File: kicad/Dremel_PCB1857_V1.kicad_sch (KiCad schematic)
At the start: 34 parts, among them P1 Conn_WallPlug, U1 EL817

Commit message: Add Tested parameter to schematics
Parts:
- *R6: Tested (none) -> BLOWN
- C2: renamed from *C2; Tested (none) -> BLOWN
- C3: value 1n -> 100n
- R11, R15: value R -> 510k; Tested (none) -> OK
- R12, R13: value R -> 300k
- R14: Tested (none) -> OK
- R4: value R -> 47k; Tested (none) -> OK
- R6: value R -> 30R; Tested (none) -> BLOWN 3k4
- R7: value R -> 160R; Tested (none) -> OK
- R8: value R -> 4R7; Tested (none) -> OK
- U1: value EL817 -> B179
- V11: renamed from *D7; value D -> IN4007; Tested (none) -> OK
- V5, V6: Tested (none) -> FAULTY
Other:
- moved on the sheet: R14, TR1_*L1

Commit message: Added secondary side to schematic
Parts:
- added *: 220u 25V, symbol Device:C_Polarized
- added * (x4), V14: D, symbol Device:D
- added *: 470u 25V, symbol Device:C_Polarized
- added BT1: Battery_Cell, symbol Device:Battery_Cell
- added C12: 1n, symbol Device:C
- added C13: 100n, symbol Device:C
- added C14: 10n, symbol Device:C
- added C15: 2.2 n, symbol Device:C
- added C6, C7, C8: C, symbol Device:C
- added C9: ~, symbol Device:C
- added N2: TL1431A, Package_SO:SOIC-8_3.9x4.9mm_P1.27mm, symbol Reference_Voltage:TL431D
- added R*, R17, R25, R31, R46, R47: ~, symbol Device:R
- added R12, R16, R18, R20, R22, R23, R29, R33, R40, R41, R42, R43, R44: R, symbol Device:R
- added R20: 2k, symbol Device:R
- added R24: 1k, symbol Device:R
- added R26: O.22 R, symbol Device:R
- added R27: 0.22 R, symbol Device:R
- added R28, R32: 10k, symbol Device:R
- added R34: 20k, symbol Device:R
- added R35: 6.04k, symbol Device:R
- added R36: 25.5k, symbol Device:R
- added R37: 12k, symbol Device:R
- added R38: 29.4k, symbol Device:R
- added R39: 360R, symbol Device:R
- added TH1: Thermistor_PTC, symbol Device:Thermistor_PTC
- added TR1_*L3: 13.63 uH 0.28 R, symbol Device:L
- added TR1_*L4: 9.77 uH 0.05 R, symbol Device:L
- added U3: LM324, symbol Amplifier_Operational:LM324
- added V12: BC546A, Package_TO_SOT_THT:TO-92_Inline, symbol Transistor_BJT:BC546
- added V15: LED, symbol Device:LED
- added V201: FKH382N, symbol Device:Q_NMOS_SGD
- L1: value L_Coupled_1423 -> 16m H 0.7 R
- TR1_*L1: value 9u31 R17 -> 9.31 uH 0.17 R
- TR1_*L2: value 3m16 2R82 -> 3.16 mH 2.82 R
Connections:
- net at *D1.2 (A), *D4.2 (A), *R6.2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: now also C6.1
- net at U1.1: now also R12.2
- net BAT-: now reaches U1.2
- net BAT-: now also *.2, BT1.2 (-), C13.2, C7.2, N2.2 (A), N2.3 (A), N2.6 (A), N2.7 (A), R23.1, R26.1, R27.1, R36.1, R43.2, TR1_*L3.1, U3.10 (+), U3.11 (V-), U3.12 (+), U3.5 (+), V15.1 (K), V201.1 (S)
- new net: C12.2, N2.8 (REF), R22.1, R23.2, R29.2
- new net: *.2 (A), C9.1, TR1_*L4.2
- new net: *.1, *.1 (K), *.2 (A), R17.2, R34.2, R46.1, R47.2
- new net: R24.1, R28.2, U3.13 (-)
- new net: R28.1, R32.2, U3.14
- new net: *.1 (K), R16.1, R18.1
- new net: *.2 (A), C8.2, TR1_*L3.2
- new net: *.1 (K), R12.1, V14.1 (K)
- new net: C15.2, U3.1, V14.2 (A)
- new net: *.2 (A), C14.1, U3.8
- new net: C14.2, R20.1
- new net: C8.1, R16.2
- new net: C12.1, N2.1 (K), R*.2, V12.2 (B)
- new net: R39.2, V15.2 (A)
- new net: U3.6 (-), U3.7
- new net: C15.1, R29.1, R31.2, U3.2 (-)
- new net: R41.2, R42.1, TH1.1
- new net: R20.2, R25.1, R33.2, R38.2, U3.9 (-)
- new net: R47.1, V201.3 (D)
- new net: C6.2, C7.1
- new net: *.1 (K), BT1.1 (+)
- new net: C9.2, R17.1
- new net: R40.1, R44.2, TH1.2
- new net L4_6: *.2, R24.2, R25.2, R26.2, R27.2, R46.2, TR1_*L4.1
- new net Pin 1: C13.1, R20.1, R22.2, R33.1, R42.2, R44.1, V12.3 (E)
- new net Pin 10: R34.1, R35.2, R36.2, R37.2, U3.3 (+)
- new net Pin 11: R35.1
- new net Pin 12: R37.1
- new net Pin 13: R31.1
- new net Pin 14: R38.1
- new net Pin 15: R20.2, V201.2 (G)
- new net Pin 3: R43.1
- new net Pin 7: R40.2
- new net Pin 8: R41.1
- new net Pin 9: R32.1, R39.1
- new net V2: *.1, R*.1, R18.2, U3.4 (V+), V12.1 (C)
- no-connect marks 0 -> 2
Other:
- note added: "1"
- note added: "2"
- note added: "3"
- note added: "4"
- note added: "5"
- note added: "6"
- note added: "7"
- note added: "8"
- note added: "All microcontroller pins checked."
- note added: "K3"
- note added: "K4"
- note added: "Unconnected microcontroller pins."
- moved on the sheet: *D1, *D2, *D3, *D4, *D5, *D6, *R6, C1, C16, C2, C3, C4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

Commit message: Add R30
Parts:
- R30: renamed from R*; value ~ -> 10k
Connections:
- net V2: now also R20.2; no longer R30.1
- net at C14.2: now also R30.2; no longer R20.1
- net at C12.1, N2.1 (K), V12.2 (B): now also R20.1; no longer R30.2
- net at R25.1, R33.2, R38.2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: now also R30.1; no longer R20.2
- net BAT- renamed GND2
- net GND2: no longer R36.1, V15.1 (K)
- new net Pin 16/4/5: R36.1, V15.1 (K)
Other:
- moved on the sheet: R20, R30

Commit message: Resolve R20 duplicate
Update README with attempt 2
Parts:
- added R3, R43: ?, symbol Device:R
- added U2: B179, Package_DIP:DIP-4_W7.62mm, symbol Isolator:EL817
- added V16: D, symbol Device:D
- C4: value 3n3 -> 3.3n
- R201: renamed from R20; value R -> 10k
- R8: value 4R7 -> 4.7R
- renumbered *R6 to R5
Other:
- note added: "COD"
- note added: "Check connections in an actual battery because this makes no sense!"
- note added: "K3 AKKU+"
- note added: "K4 AKKU-"
- note added: "NTC"
- note removed: "K3"
- note removed: "K4"
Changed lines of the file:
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@@
     (stroke (width 0) (type default))
   )
+  (rectangle (start 381 49.53) (end 420.37 95.25)
+    (stroke (width 0) (type default))
+    (fill (type none))
+  )
   (text "Unconnected microcontroller pins." (at 27.94 163.83 0)
     (effects (font (size 1.27 1.27)) (justify left bottom))
@@
     (effects (font (size 1.27 1.27)) (justify left bottom))
   )
+  (text "Check connections in an actual battery because this makes no sense!"
+    (at 381 97.79 0)
+    (effects (font (size 1.27 1.27)) (justify left bottom))
+  )
   (text "6" (at 154.94 48.26 0)
     (effects (font (size 1.27 1.27)) (justify left bottom))
   )
-  (text "K3" (at 236.22 67.31 0)
+  (text "K3 AKKU+" (at 236.22 67.31 0)
+    (effects (font (size 1.27 1.27)) (justify left bottom))
+  )
+  (text "COD" (at 402.59 64.77 0)
+    (effects (font (size 1.27 1.27)) (justify left bottom))
+  )
+  (text "NTC" (at 402.59 76.2 0)
     (effects (font (size 1.27 1.27)) (justify left bottom))
   )
@@
     (effects (font (size 1.27 1.27)) (justify left bottom))
   )
-  (text "K4" (at 236.22 76.2 0)
+  (text "K4 AKKU-" (at 236.22 76.2 0)
     (effects (font (size 1.27 1.27)) (justify left bottom))
   )
@@
   (symbol (lib_id "Device:R") (at 109.22 102.87 0) (unit 1)
     (in_bom yes) (on_board yes) (dnp no)
-    (property "Reference" "*R6" (at 111.76 102.235 0)
+    (property "Reference" "R5" (at 111.76 102.235 0)
       (effects (font (size 1.27 1.27)) (justify left))
     )
@@
       (project "Dremel_PCB1857_V1"
         (path "/ab18b4c8-6f40-44db-bccd-b69c22b3ada9"
-          (reference "*R6") (unit 1)
+          (reference "R5") (unit 1)
         )
       )
@@
     )
   )
+  (symbol (lib_id "Isolator:EL817") (at 87.63 142.24 180) (unit 1)
+    (in_bom yes) (on_board yes) (dnp yes)
+    (property "Reference" "U2" (at 83.82 137.16 0)
+      (effects (font (size 1.27 1.27)))
+    )
+    (property "Value" "B179" (at 87.63 147.32 0)
+      (effects (font (size 1.27 1.27)))
+    )
+    (property "Footprint" "Package_DIP:DIP-4_W7.62mm" (at 92.71 137.16 0)
+      (effects (font (size 1.27 1.27) italic) (justify left) hide)
+    )
+    (property "Datasheet" "http://www.everlight.com/file/ProductFile/EL817.pdf" (at 87.63 142.24 0)
+      (effects (font (size 1.27 1.27)) (justify left) hide)
+    )
+    (pin "1")
+    (pin "2")
+    (pin "3")
+    (pin "4")
+    (instances
+      (project "Dremel_PCB1857_V1"
+        (path "/ab18b4c8-6f40-44db-bccd-b69c22b3ada9"
+          (reference "U2") (unit 1)
+        )
+      )
+    )
+  )
   (symbol (lib_id "Device:Q_NMOS_SGD") (at 267.97 71.12 0) (mirror y) (unit 1)
     (in_bom yes) (on_board yes) (dnp no)
@@
       (effects (font (size 1.27 1.27)))
     )
-    (property "Value" "4R7" (at 93.98 104.14 0)
+    (property "Value" "4.7R" (at 93.98 104.14 0)
       (effects (font (size 1.27 1.27)))
     )
@@
   (symbol (lib_id "Device:R") (at 285.75 71.12 270) (unit 1)
     (in_bom yes) (on_board yes) (dnp no) (fields_autoplaced)
-    (property "Reference" "R20" (at 285.75 66.04 90)
-      (effects (font (size 1.27 1.27)))
-    )
-    (property "Value" "R" (at 285.75 68.58 90)
+    (property "Reference" "R201" (at 285.75 66.04 90)
+      (effects (font (size 1.27 1.27)))
+    )
+    (property "Value" "10k" (at 285.75 68.58 90)
       (effects (font (size 1.27 1.27)))
     )
@@
       (project "Dremel_PCB1857_V1"
         (path "/ab18b4c8-6f40-44db-bccd-b69c22b3ada9"
-          (reference "R20") (unit 1)
+          (reference "R201") (unit 1)
         )
       )
@@
     )
   )
+  (symbol (lib_id "Device:R") (at 57.15 142.24 180) (unit 1)
+    (in_bom yes) (on_board yes) (dnp yes)
+    (property "Reference" "R3" (at 62.23 140.97 0)
+      (effects (font (size 1.27 1.27)))
+    )
+    (property "Value" "?" (at 62.23 143.51 0)
+      (effects (font (size 1.27 1.27)))
+    )
+    (property "Footprint" "" (at 58.928 142.24 90)
+      (effects (font (size 1.27 1.27)) hide)
+    )
+    (property "Datasheet" "~" (at 57.15 142.24 0)
+      (effects (font (size 1.27 1.27)) hide)
+    )
+    (pin "1")
+    (pin "2")
+    (instances
+      (project "Dremel_PCB1857_V1"
+        (path "/ab18b4c8-6f40-44db-bccd-b69c22b3ada9"
+          (reference "R3") (unit 1)
+        )
+      )
+    )
+  )
   (symbol (lib_id "Device:C") (at 99.06 54.61 0) (unit 1)
     (in_bom yes) (on_board yes) (dnp no) (fields_autoplaced)
@@
       (effects (font (size 1.27 1.27)) (justify left))
     )
-    (property "Value" "3n3" (at 102.87 56.515 0)
+    (property "Value" "3.3n" (at 102.87 56.515 0)
       (effects (font (size 1.27 1.27)) (justify left))
     )
@@
     )
   )
+  (symbol (lib_id "Device:R") (at 34.29 143.51 180) (unit 1)
+    (in_bom yes) (on_board yes) (dnp yes)
+    (property "Reference" "R43" (at 39.37 142.24 0)
+      (effects (font (size 1.27 1.27)))
+    )
+    (property "Value" "?" (at 39.37 144.78 0)
+      (effects (font (size 1.27 1.27)))
+    )
+    (property "Footprint" "" (at 36.068 143.51 90)
+      (effects (font (size 1.27 1.27)) hide)
+    )
+    (property "Datasheet" "~" (at 34.29 143.51 0)
+      (effects (font (size 1.27 1.27)) hide)
+    )
+    (pin "1")
+    (pin "2")
+    (instances
+      (project "Dremel_PCB1857_V1"
+        (path "/ab18b4c8-6f40-44db-bccd-b69c22b3ada9"
+          (reference "R43") (unit 1)
+        )
+      )
+    )
+  )
   (symbol (lib_id "Device:R") (at 387.35 -16.51 0) (mirror y) (unit 1)
     (in_bom yes) (on_board yes) (dnp no)
@@
         )
       )
+    )
+  )
+  (symbol (lib_id "Device:D") (at 110.49 142.24 0) (mirror y) (unit 1)
+    (in_bom yes) (on_board yes) (dnp yes) (fields_autoplaced)
+    (property "Reference" "V16" (at 110.49 139.7 0)
+      (effects (font (size 1.27 1.27)))
+    )
+    (property "Value" "D" (at 108.585 139.7 90)
+      (effects (font (size 1.27 1.27)) (justify left) hide)
+    )
+    (property "Footprint" "" (at 110.49 142.24 0)
+      (effects (font (size 1.27 1.27)) hide)
+    )
+    (property "Datasheet" "~" (at 110.49 142.24 0)
+      (effects (font (size 1.27 1.27)) hide)
+    )
+    (property "Sim.Device" "D" (at 110.49 142.24 0)
+      (effects (font (size 1.27 1.27)) hide)
+    )
+    (property "Sim.Pins" "1=K 2=A" (at 110.49 142.24 0)
+      (effects (font (size 1.27 1.27)) hide)
+    )
+    (pin "1")
+    (pin "2")
+    (instances
+      (project "Dremel_PCB1857_V1"
+        (path "/ab18b4c8-6f40-44db-bccd-b69c22b3ada9"
+          (reference "V16") (unit 1)
+        )
+      )

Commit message: Tidy up main side layout
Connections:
- net GND2: no longer U1.2
- net at *.2 (A), C8.2, TR1_*L3.2: now also U1.2
- net at *.1 (K), V14.1 (K): now also R12.2; no longer R12.1
- net feedback: now reaches U1.1
- net feedback: now also R12.1; no longer R12.2
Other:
- moved on the sheet: *D6, C16, C3, C5, C6, C7, R12, R14, R3, R4, R43, R5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

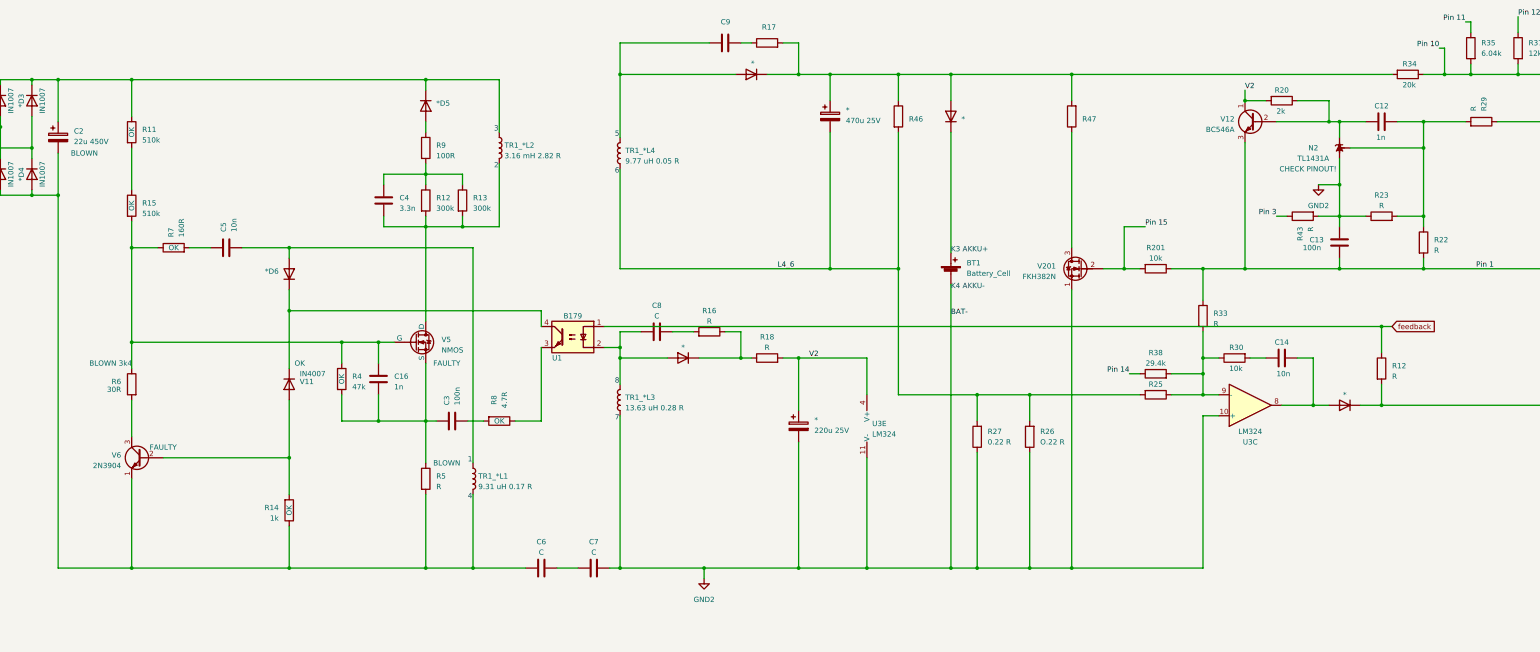
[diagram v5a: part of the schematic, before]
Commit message: Add R10 and V11 connection
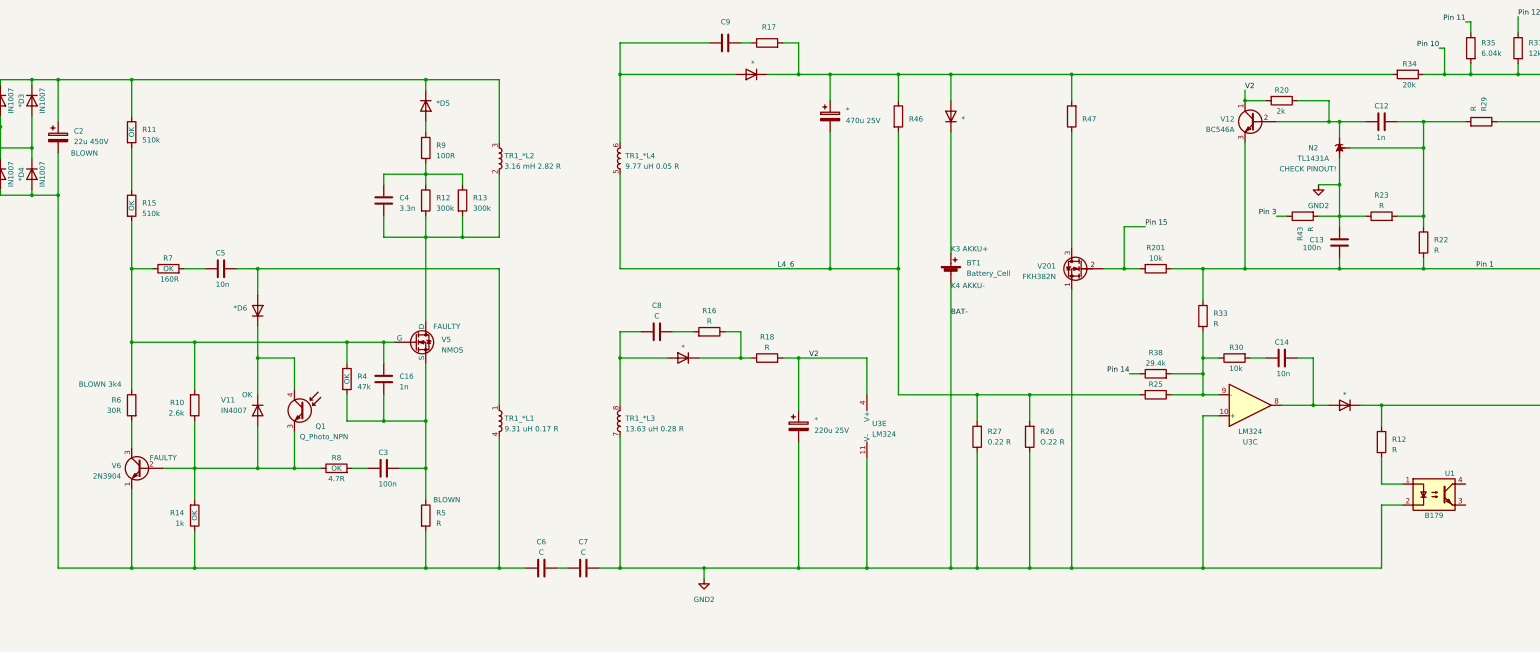
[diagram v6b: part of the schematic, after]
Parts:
- added Q1: Q_Photo_NPN, symbol Device:Q_Photo_NPN
- added R10: 2.6k, symbol Device:R
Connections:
- net GND2: now also TR1_*L3.7, U1.2; no longer TR1_*L3.1
- net L4_6: now also TR1_*L4.5; no longer TR1_*L4.1
- net at C16.1, R15.2, R4.1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: now also R10.2
- net at *.2 (A), C9.1: now also TR1_*L4.6; no longer TR1_*L4.2
- net at *D1.2 (A), *D4.2 (A), C2.2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: now also TR1_*L1.4; no longer TR1_*L1.2
- net at *.2 (A), C8.2: now also TR1_*L3.8; no longer TR1_*L3.2, U1.2
- net at *.1 (K), V14.1 (K): now also R12.1; no longer R12.2
- net at *D2.1 (K), *D3.1 (K), *D5.1 (K)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: now also TR1_*L2.3; no longer TR1_*L2.1
- net at R14.2, V11.2 (A), V6.2 (B): now also R8.1, Q1.3 (E), R10.1
- net at U1.3: no longer R8.1
- net at *D6.1 (K), V11.1 (K): now also Q1.4 (C); no longer U1.4
- net feedback: no longer names the net of U1.1
- net feedback: now also R12.2; no longer R12.1
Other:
- note removed: "1"
- note removed: "2"
- note removed: "3"
- note removed: "4"
- note removed: "5"
- note removed: "6"
- note removed: "7"
- note removed: "8"
- moved on the sheet: *D6, C16, C3, C5, C7, R12, R14, R4, R5, R6, R7, R8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

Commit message: Split schematic into mutliple hierachical sheets
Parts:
- removed *: 220u 25V, symbol Device:C_Polarized
- removed * (x4), *D5, *D6, V14, V16: D, symbol Device:D
- removed *: 470u 25V, symbol Device:C_Polarized
- removed *D1, *D2, *D3, *D4: IN1007, symbol Device:D
- removed BT1: Battery_Cell, symbol Device:Battery_Cell
- removed C1: 470n X2, symbol Device:C
- removed C12, C16: 1n, symbol Device:C
- removed C13, C3: 100n, symbol Device:C
- removed C14, C5: 10n, symbol Device:C
- removed C15: 2.2 n, symbol Device:C
- removed C2: 22u 450V, symbol Device:C_Polarized
- removed C4: 3.3n, symbol Device:C
- removed C6, C7, C8: C, symbol Device:C
- removed C9: ~, symbol Device:C
- removed F1: Fuse, symbol Device:Fuse
- removed L1: 16m H 0.7 R, symbol Device:L_Coupled_1423
- removed N2: TL1431A, Package_SO:SOIC-8_3.9x4.9mm_P1.27mm, symbol Reference_Voltage:TL431D
- removed P1: Conn_WallPlug, symbol Connector:Conn_WallPlug
- removed Q1: Q_Photo_NPN, symbol Device:Q_Photo_NPN
- removed R1, TH1: Thermistor_PTC, symbol Device:Thermistor_PTC
- removed R10: 2.6k, symbol Device:R
- removed R11, R15: 510k, symbol Device:R
- removed R12, R13: 300k, symbol Device:R
- removed R12, R16, R18, R22, R23, R29, R33, R40, R41, R42, R43, R44, R5: R, symbol Device:R
- removed R14, R24: 1k, symbol Device:R
- removed R17, R25, R31, R46, R47: ~, symbol Device:R
- removed R2: 680K, symbol Device:R
- removed R20: 2k, symbol Device:R
- removed R201, R28, R30, R32: 10k, symbol Device:R
- removed R26: O.22 R, symbol Device:R
- removed R27: 0.22 R, symbol Device:R
- removed R3, R43: ?, symbol Device:R
- removed R34: 20k, symbol Device:R
- removed R35: 6.04k, symbol Device:R
- removed R36: 25.5k, symbol Device:R
- removed R37: 12k, symbol Device:R
- removed R38: 29.4k, symbol Device:R
- removed R39: 360R, symbol Device:R
- removed R4: 47k, symbol Device:R
- removed R6: 30R, symbol Device:R
- removed R7: 160R, symbol Device:R
- removed R8: 4.7R, symbol Device:R
- removed R9: 100R, symbol Device:R
- removed TR1_*L1: 9.31 uH 0.17 R, symbol Device:L
- removed TR1_*L2: 3.16 mH 2.82 R, symbol Device:L
- removed TR1_*L3: 13.63 uH 0.28 R, symbol Device:L
- removed TR1_*L4: 9.77 uH 0.05 R, symbol Device:L
- removed U1, U2: B179, Package_DIP:DIP-4_W7.62mm, symbol Isolator:EL817
- removed U3: LM324, symbol Amplifier_Operational:LM324
- removed V11: IN4007, symbol Device:D
- removed V12: BC546A, Package_TO_SOT_THT:TO-92_Inline, symbol Transistor_BJT:BC546
- removed V15: LED, symbol Device:LED
- removed V201: FKH382N, symbol Device:Q_NMOS_SGD
- removed V5: NMOS, symbol Simulation_SPICE:NMOS
- removed V6: 2N3904, Package_TO_SOT_THT:TO-92_Inline, symbol Transistor_BJT:2N3904
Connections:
- no-connect marks 2 -> 0
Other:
- added sheet Battery (battery.kicad_sch)
- added sheet Mains side (mains_side.kicad_sch)
- added sheet Secondary side (secondary_side.kicad_sch)
- note removed: "All microcontroller pins checked."
- note removed: "COD"
- note removed: "Check connections in an actual battery because this makes no sense!"
- note removed: "K3 AKKU+"
- note removed: "K4 AKKU-"
- note removed: "NTC"
- note removed: "Unconnected microcontroller pins."

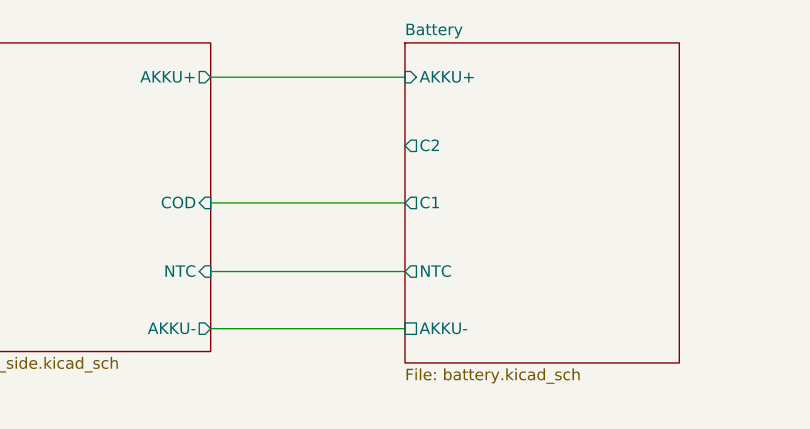
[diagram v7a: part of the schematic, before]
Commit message: Add footprints
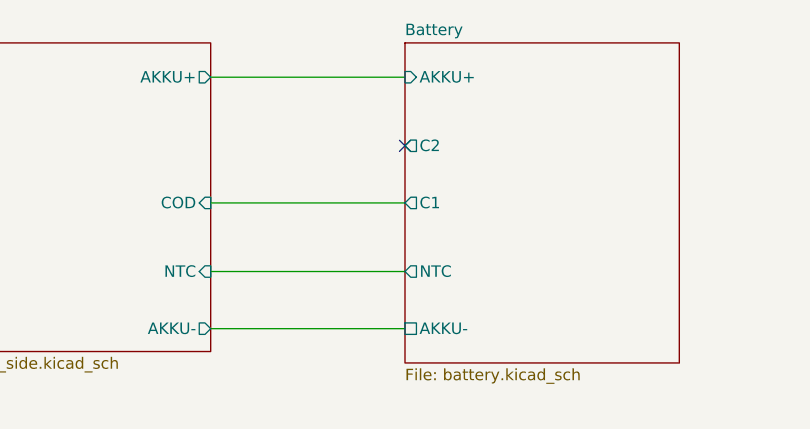
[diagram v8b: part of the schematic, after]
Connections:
- no-connect marks 0 -> 1
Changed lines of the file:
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@@
 (kicad_sch (version 20230121) (generator eeschema)
   (paper "A4")
+  (no_connect (at 187.96 81.28))
   (wire (pts (xy 110.49 100.33) (xy 129.54 100.33))
     (stroke (width 0) (type default))
